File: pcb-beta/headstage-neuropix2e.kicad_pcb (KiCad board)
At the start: 4 copper layers, 60 x 60 mm, 64 parts, among them J1 X.FL-R-SMT-1(02), J2 046844727002846+, J3 046844727002846+, J4 SBH11-PBPC-D05-ST-BK, J5 TC2030, J6 050700622, U1 MIC5335-JGYMT, U2 NCP163AFCT180T2G, U3 DS90UB933TRTVTQ1, U4 TS5A3159AYZPR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

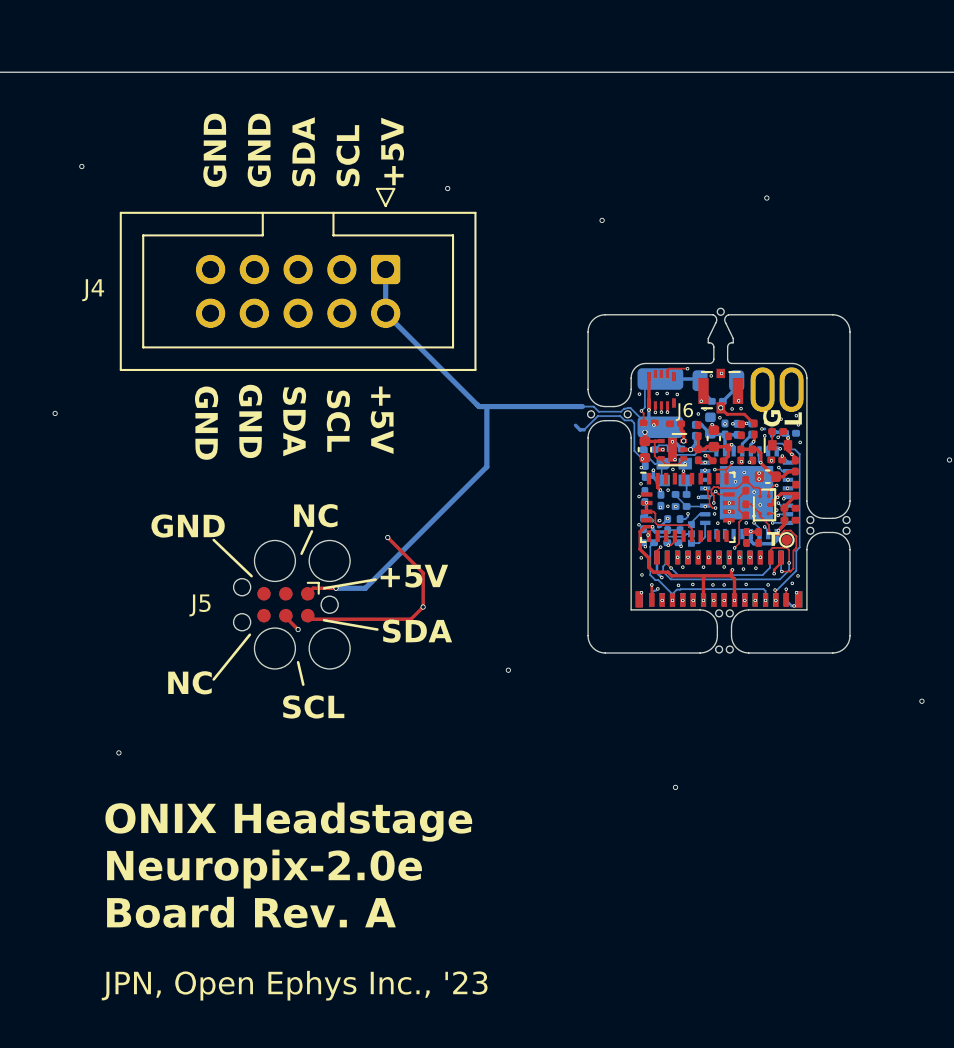
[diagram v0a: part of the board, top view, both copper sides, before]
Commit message: Move pcb to pcb-beta directory
- Because this board only works with Beta-test NP2.0 probes
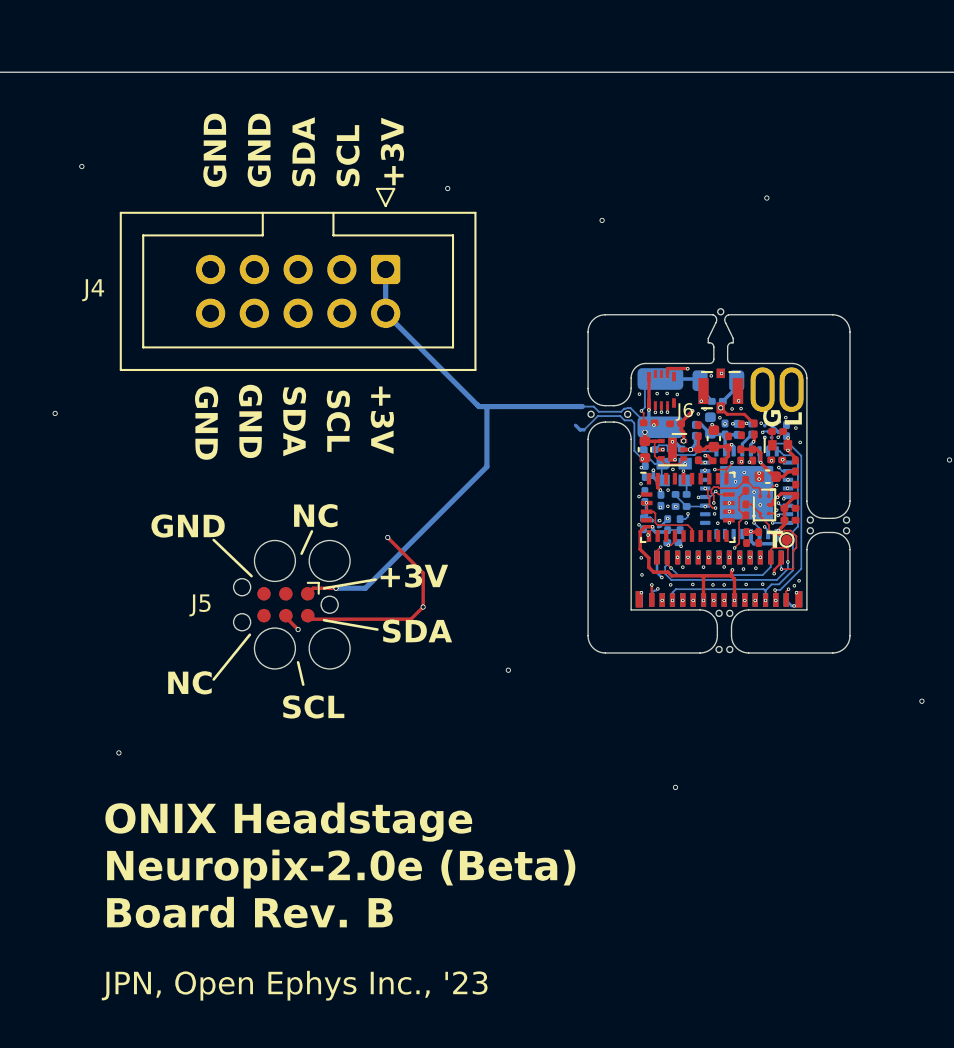
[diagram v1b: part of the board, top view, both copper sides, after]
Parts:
- removed JP1: Jumper_3_Bridged12, jonnew:OE_SolderJumper-3_0201_Bridged12
- removed R8: 10k, Resistor_SMD:R_0201_0603Metric
- U6: value CAT24C04C4ATR -> M24C64-FCS6TP/K; footprint jonnew:ONSEMI_567JZ_WLCSP4-0.84x0.86 -> jonnew:ST_WLCSP5-0.959x1.073
- moved C25 0.28 mm to (146.3, 85.8), turned to -90 degrees
- moved U6 0.05 mm to (145.3, 85.8), turned to 180 degrees
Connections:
- net /Neuropixels 2.0/NP_{RESET} renamed /Neuropixels 2.0/NP_{~{RST}}
- J2 pad 23: /Neuropixels 2.0/SYNC -> /Neuropixels 2.0/NP_{~{MUXRST}}
- J2 pad 5: /Neuropixels 2.0/SYNC -> /Neuropixels 2.0/NP_{~{MUXRST}}
- J3 pad 23: /Neuropixels 2.0/SYNC -> /Neuropixels 2.0/NP_{~{MUXRST}}
- J3 pad 5: /Neuropixels 2.0/SYNC -> /Neuropixels 2.0/NP_{~{MUXRST}}
- J6 pad 6: /Perpherials/GPIO -> +2V5
- R4 pad 1: /Perpherials/GPIO -> /Neuropixels 2.0/NP_{Select}
- U3 pad 1: Net-(JP1-A) -> unconnected-(U3-HSYNC-Pad1)
- U3 pad 16: /Neuropixels 2.0/NP_{Select} -> /Neuropixels 2.0/NP_{~{MUXRST}}
- U3 pad 17: /Perpherials/GPIO -> /Neuropixels 2.0/NP_{Select}
- U3 pad 2: Net-(JP1-B) -> unconnected-(U3-VSYNC-Pad2)
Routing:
- net /Neuropixels 2.0/NP_{~{MUXRST}}: track 0.00 -> 16.6 mm, vias 0 -> 2
- net /Neuropixels 2.0/SYNC: track 12.8 -> 0.00 mm, vias 2 -> 0
- net /Perpherials/GPIO: track 12.2 -> 0.00 mm, vias 2 -> 0
- net +2V5: track 13.0 -> 18.1 mm, vias 2 -> 4
- net Net-(JP1-A): track 1.78 -> 0.00 mm
- net +1V8: track 41.7 -> 40.0 mm, vias 12 -> 11
- net Net-(JP1-B): track 1.13 -> 0.00 mm
- net /Neuropixels 2.0/NP_{Select}: track 3.79 -> 2.98 mm
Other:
- outline, holes or cut-outs redrawn
- board text added: "+3V"
- board text added: "ONIX Headstage Neuropix-2.0e (Beta) Board Rev. B"
- board text removed: "+5V"
- board text removed: "ONIX Headstage Neuropix-2.0e Board Rev. A"

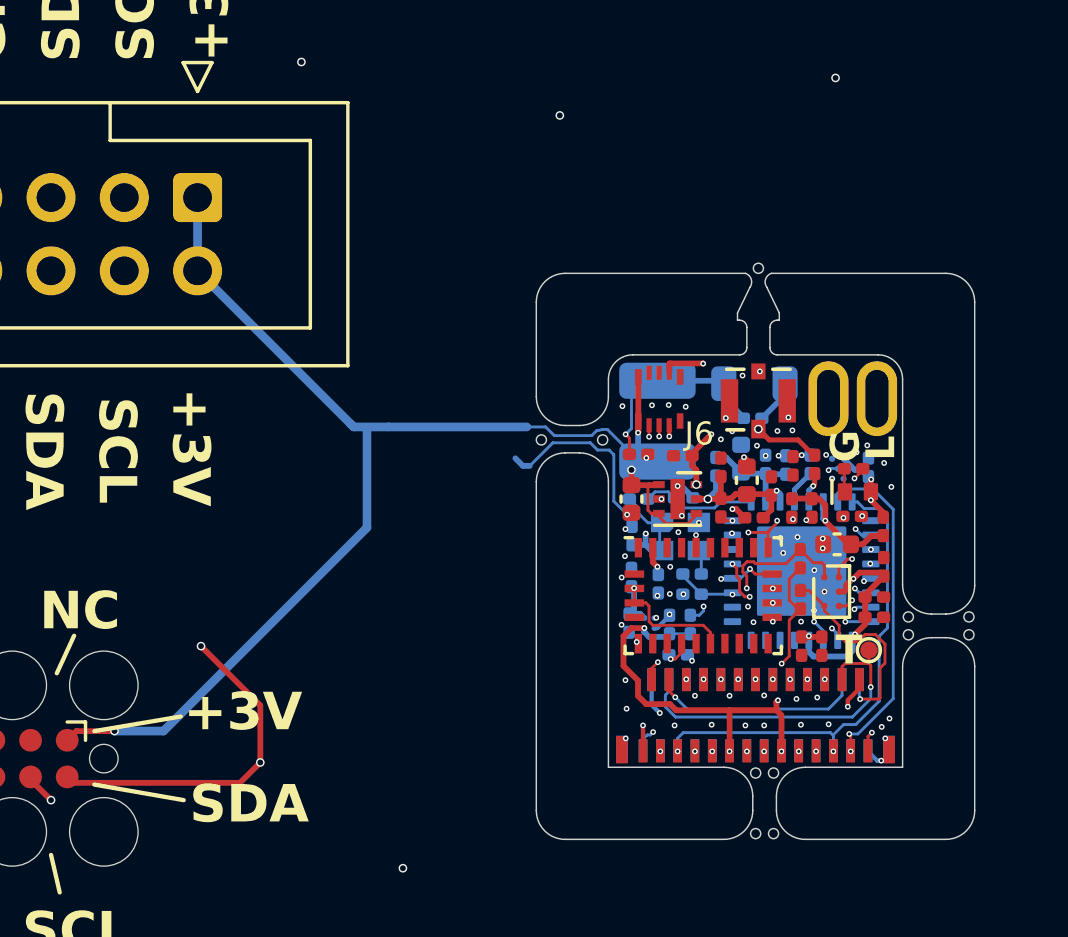
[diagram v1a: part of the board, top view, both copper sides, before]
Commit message: Revision B (Beta)
- Neuropixels 2.0 headstage for beta-test probes
- Updated PCB specs to match the headstage for publically avaiable
  probes (increase via size to 0.25/0.15)
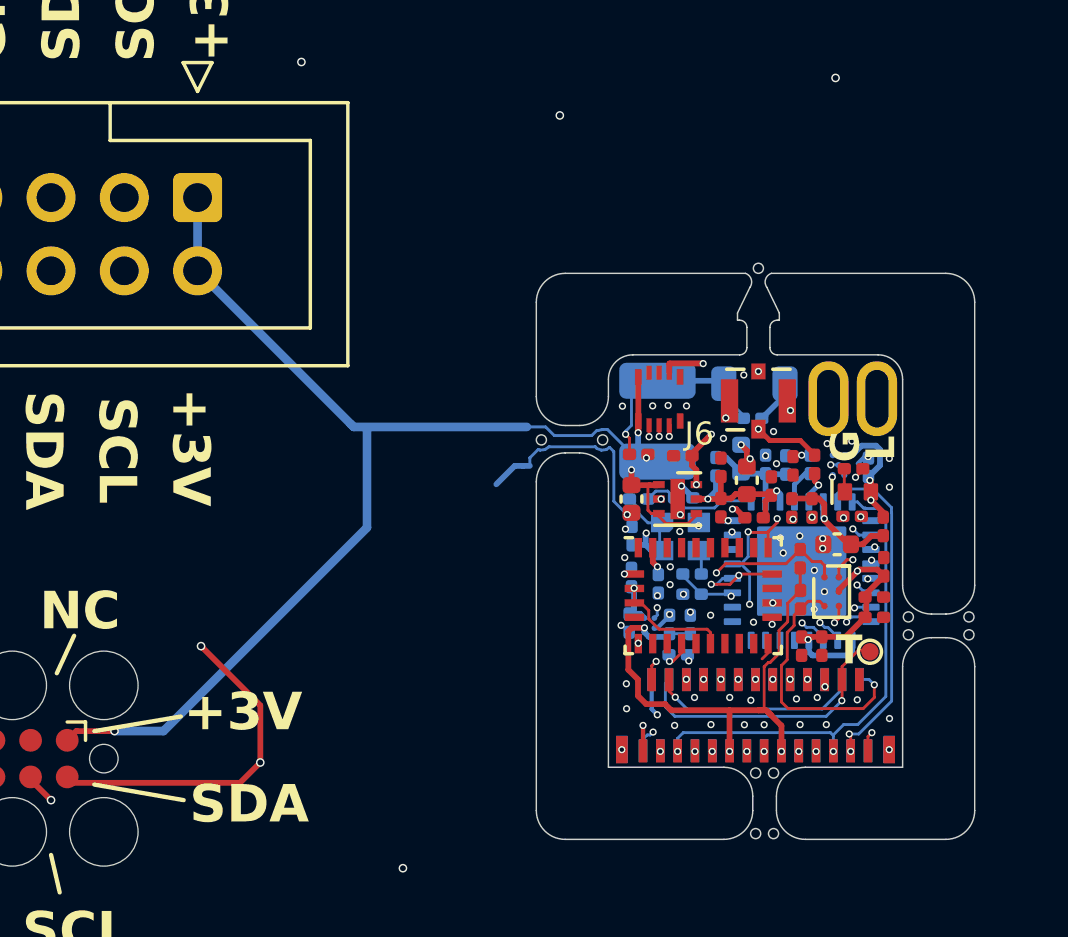
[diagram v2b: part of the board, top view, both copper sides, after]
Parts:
- moved U6 0.13 mm to (145.3, 85.7)
- moved TP3 0.07 mm to (146.4, 92.2)
- turned R10 to -90 degrees
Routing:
- net +1V8: track 40.0 -> 42.9 mm, vias 11 -> 10
- net /Neuropixels 2.0/NP_{TP1}: track 11.7 -> 9.82 mm
- net /Neuropixels 2.0/SDA_{B}: track 7.55 -> 9.02 mm
- net /Neuropixels 2.0/D2: track 6.58 -> 5.72 mm
- net /Neuropixels 2.0/D6: track 6.60 -> 5.79 mm
- net GND: track 13.0 -> 13.7 mm, vias 98 -> 91
- net /Neuropixels 2.0/SDA: track 68.8 -> 68.5 mm, vias 9 -> 8
- net +1.8VA: track 18.5 -> 18.4 mm, vias 5 -> 3
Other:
- board text added: "rB"
- board text removed: "rA"
